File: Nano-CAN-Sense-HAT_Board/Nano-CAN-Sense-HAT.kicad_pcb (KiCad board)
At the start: 4 copper layers, 46 x 20 mm, 48 parts, among them J1 Analog, J2 Digital, J3 Conn_02x04_Counter_Clockwise, J4 Conn_02x04_Counter_Clockwise, J5 Conn_01x05, J6 Conn_01x03, SW1 SW_Push, SW2 SW_Push, U1 LMC6484, U2 MCP2518FD-xQBB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

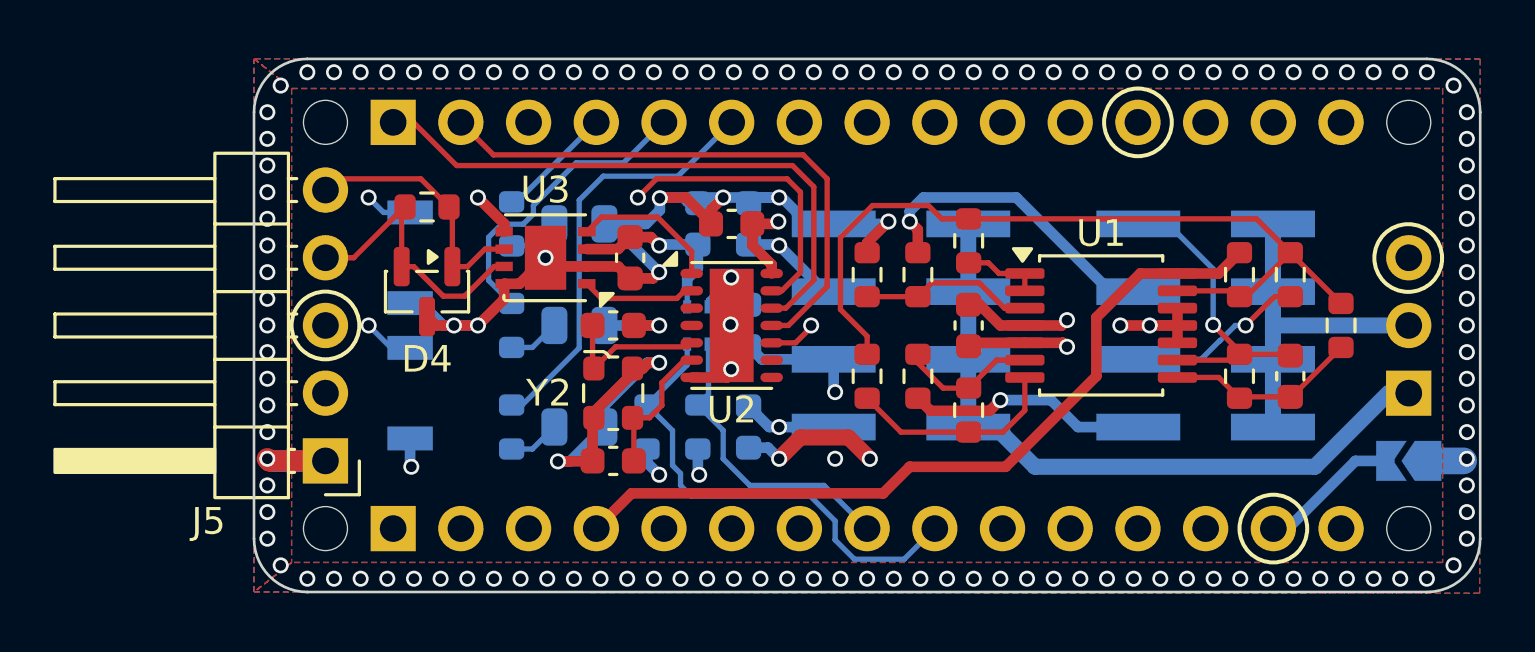
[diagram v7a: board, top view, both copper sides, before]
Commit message: power distribution using copper pours Gitignore *.zip
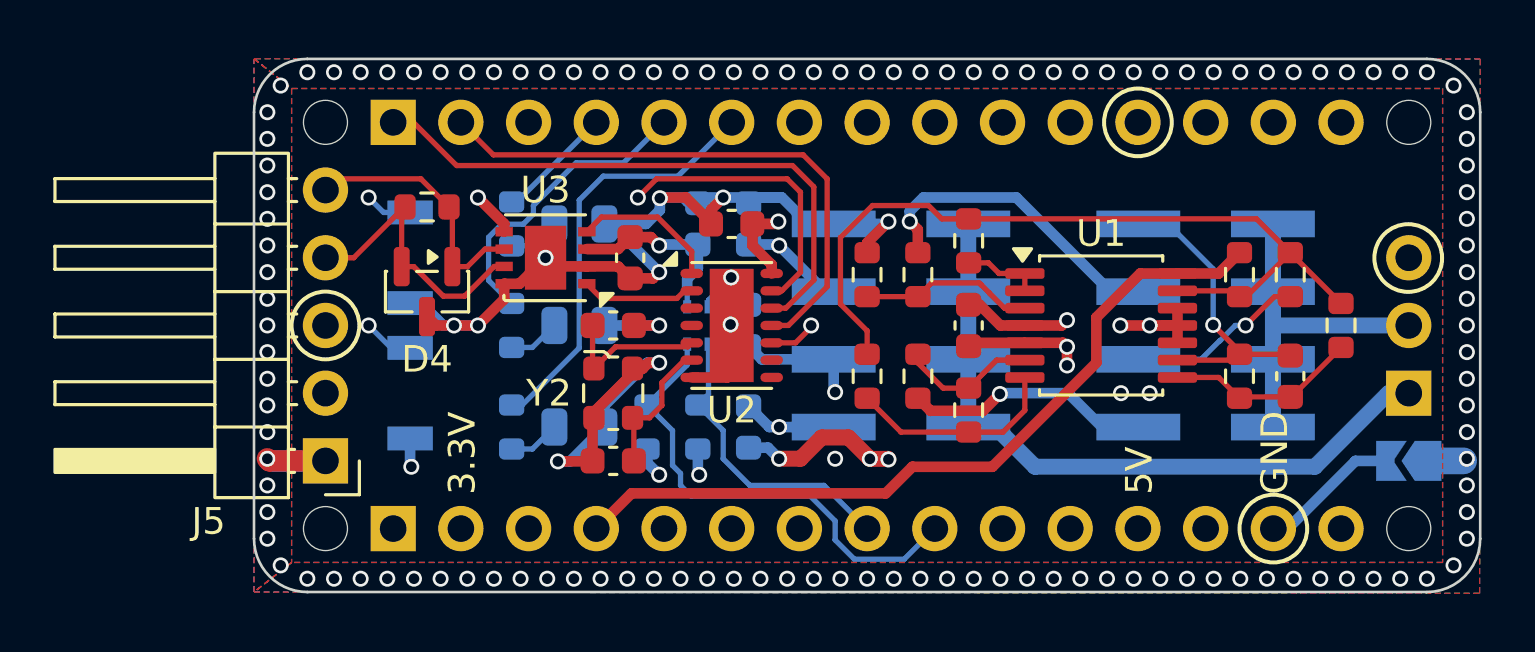
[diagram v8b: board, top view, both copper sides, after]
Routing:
- net +5V: track 80.3 -> 37.4 mm, vias 8 -> 10
- net +3V3: track 17.7 -> 7.10 mm
- net GND: track 82.7 -> 84.1 mm
- added copper zone on In2.Cu, net +3V3
- added copper zone on In2.Cu, net +5V
